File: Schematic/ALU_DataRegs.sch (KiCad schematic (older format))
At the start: 3 parts, among them IC4 74HCT574, IC5 74HCT574, IC6 M27C322-100F1

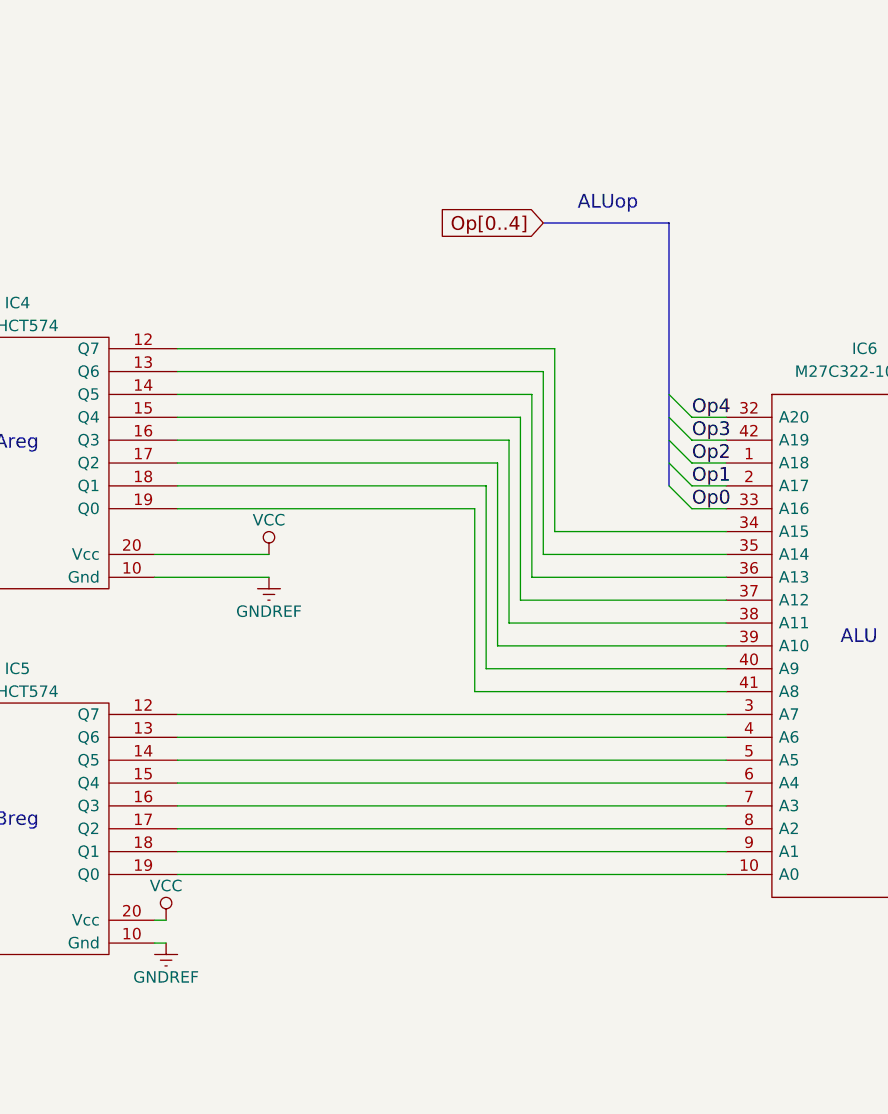
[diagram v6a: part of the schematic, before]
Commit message: Brought the PCB up to date with the new schematic, and tested the RAM with a test program.
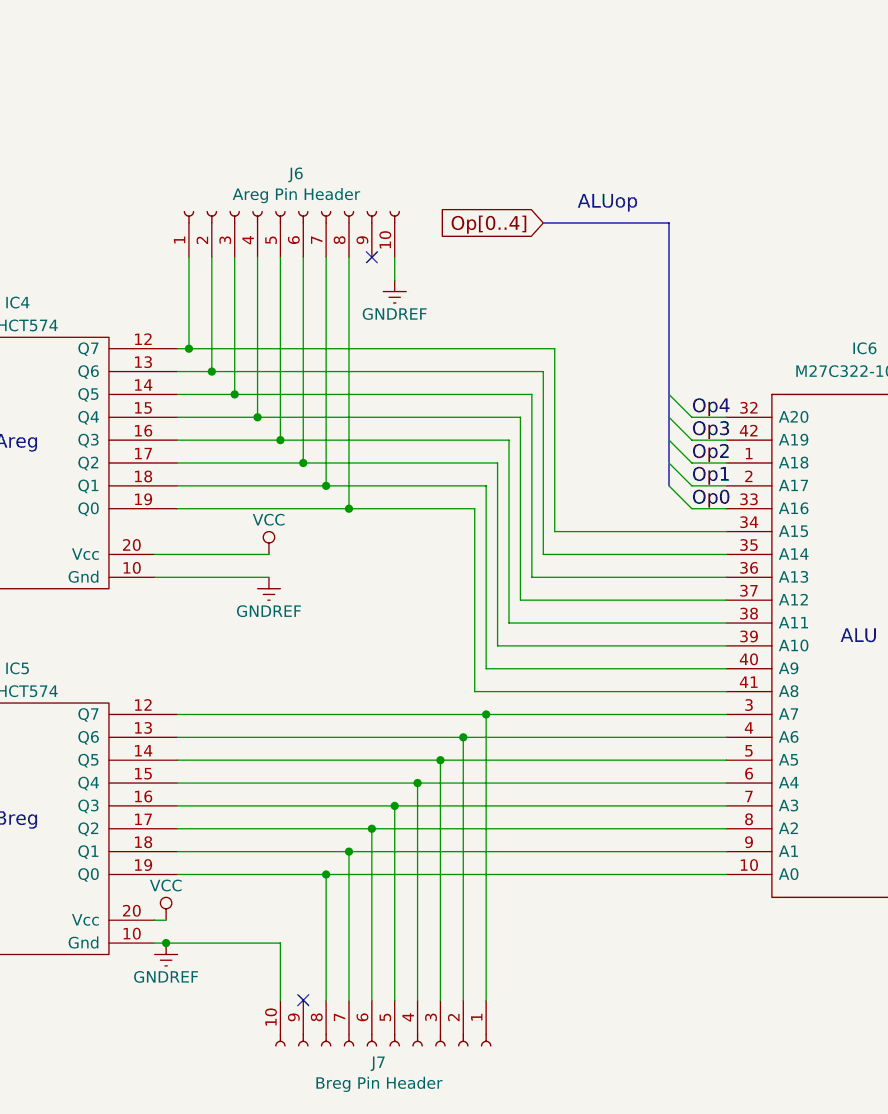
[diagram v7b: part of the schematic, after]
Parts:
- added J6: Areg Pin Header, Connector_PinSocket_2.54mm:PinSocket_1x10_P2.54mm_Vertical, symbol Connector:Conn_01x10_Female
- added J7: Breg Pin Header, Connector_PinSocket_2.54mm:PinSocket_1x10_P2.54mm_Vertical, symbol Connector:Conn_01x10_Female
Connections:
- net GNDREF: now also J6.10 (Pin_10), J7.10 (Pin_10)
- net at IC5.19 (Q0), IC6.10 (A0): now also J7.8 (Pin_8)
- net at IC5.12 (Q7), IC6.3 (A7): now also J7.1 (Pin_1)
- net at IC4.12 (Q7), IC6.34 (A15): now also J6.1 (Pin_1)
- net at IC4.13 (Q6), IC6.35 (A14): now also J6.2 (Pin_2)
- net at IC4.14 (Q5), IC6.36 (A13): now also J6.3 (Pin_3)
- net at IC4.15 (Q4), IC6.37 (A12): now also J6.4 (Pin_4)
- net at IC4.16 (Q3), IC6.38 (A11): now also J6.5 (Pin_5)
- net at IC4.17 (Q2), IC6.39 (A10): now also J6.6 (Pin_6)
- net at IC5.13 (Q6), IC6.4 (A6): now also J7.2 (Pin_2)
- net at IC4.18 (Q1), IC6.40 (A9): now also J6.7 (Pin_7)
- net at IC4.19 (Q0), IC6.41 (A8): now also J6.8 (Pin_8)
- net at IC5.14 (Q5), IC6.5 (A5): now also J7.3 (Pin_3)
- net at IC5.15 (Q4), IC6.6 (A4): now also J7.4 (Pin_4)
- net at IC5.16 (Q3), IC6.7 (A3): now also J7.5 (Pin_5)
- net at IC5.17 (Q2), IC6.8 (A2): now also J7.6 (Pin_6)
- net at IC5.18 (Q1), IC6.9 (A1): now also J7.7 (Pin_7)
- no-connect marks 3 -> 5
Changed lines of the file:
@@
 $EndComp
 Wire Wire Line
-	4500 4500 6900 4500
-Wire Wire Line
-	4500 4600 6900 4600
-Wire Wire Line
-	4500 4700 6900 4700
-Wire Wire Line
-	4500 4800 6900 4800
-Wire Wire Line
-	4500 4900 6900 4900
-Wire Wire Line
-	4500 5000 6900 5000
-Wire Wire Line
-	4500 5100 6900 5100
-Wire Wire Line
-	4500 5200 6900 5200
+	4500 4500 5850 4500
+Wire Wire Line
+	4500 4600 5750 4600
+Wire Wire Line
+	4500 4700 5650 4700
+Wire Wire Line
+	4500 4800 5550 4800
 Wire Wire Line
 	6150 3700 6900 3700
 Wire Wire Line
-	4500 2900 6150 2900
-Wire Wire Line
 	6100 3800 6900 3800
 Wire Wire Line
-	4500 3000 6100 3000
-Wire Wire Line
-	4500 3100 6050 3100
-Wire Wire Line
 	6050 3900 6900 3900
 Wire Wire Line
-	4500 3200 6000 3200
-Wire Wire Line
 	6000 4000 6900 4000
 Wire Wire Line
-	4500 3300 5950 3300
-Wire Wire Line
 	5950 4100 6900 4100
 Wire Wire Line
-	4500 3400 5900 3400
-Wire Wire Line
 	5900 4200 6900 4200
 Wire Wire Line
-	4500 3500 5850 3500
-Wire Wire Line
 	5850 4300 6900 4300
-Wire Wire Line
-	4500 3600 5800 3600
 Wire Wire Line
 	5800 4400 6900 4400
@@
 Wire Wire Line
 	8300 3300 8650 3300
+$Comp
+L Connector:Conn_01x10_Female J7
+U 1 1 5CD2E273
+P 5450 5950
+F 0 "J7" V 5523 5880 50  0000 C CNN
+F 1 "Breg Pin Header" V 5614 5880 50  0000 C CNN
+F 2 "Connector_PinSocket_2.54mm:PinSocket_1x10_P2.54mm_Vertical" H 5450 5950 50  0001 C CNN
+F 3 "~" H 5450 5950 50  0001 C CNN
+	1    5450 5950
+	0    1    1    0
+$EndComp
+Wire Wire Line
+	5850 5750 5850 4500
+Connection ~ 5850 4500
+Wire Wire Line
+	5850 4500 6900 4500
+Wire Wire Line
+	5750 5750 5750 4600
+Connection ~ 5750 4600
+Wire Wire Line
+	5750 4600 6900 4600
+Wire Wire Line
+	5650 5750 5650 4700
+Connection ~ 5650 4700
+Wire Wire Line
+	5650 4700 6900 4700
+Wire Wire Line
+	4500 5200 5150 5200
+Wire Wire Line
+	4500 5100 5250 5100
+Wire Wire Line
+	4500 5000 5350 5000
+Wire Wire Line
+	4500 4900 5450 4900
+Wire Wire Line
+	5550 5750 5550 4800
+Connection ~ 5550 4800
+Wire Wire Line
+	5550 4800 6900 4800
+Wire Wire Line
+	5450 5750 5450 4900
+Connection ~ 5450 4900
+Wire Wire Line
+	5450 4900 6900 4900
+Wire Wire Line
+	5350 5750 5350 5000
+Connection ~ 5350 5000
+Wire Wire Line
+	5350 5000 6900 5000
+Wire Wire Line
+	5250 5750 5250 5100
+Connection ~ 5250 5100
+Wire Wire Line
+	5250 5100 6900 5100
+Wire Wire Line
+	5150 5750 5150 5200
+Connection ~ 5150 5200
+Wire Wire Line
+	5150 5200 6900 5200
+NoConn ~ 5050 5750
+Wire Wire Line
+	4450 5500 4950 5500
+Wire Wire Line
+	4950 5500 4950 5750
+Connection ~ 4450 5500
+$Comp
+L Connector:Conn_01x10_Female J6
+U 1 1 5CD78577
+P 4950 2300
+F 0 "J6" V 5115 2230 50  0000 C CNN
+F 1 "Areg Pin Header" V 5024 2230 50  0000 C CNN
+F 2 "Connector_PinSocket_2.54mm:PinSocket_1x10_P2.54mm_Vertical" H 4950 2300 50  0001 C CNN
+F 3 "~" H 4950 2300 50  0001 C CNN
+	1    4950 2300
+	0    -1   -1   0
+$EndComp
+NoConn ~ 5350 2500
+$Comp
+L power:GNDREF #PWR0103
+U 1 1 5CDA8761
+P 5450 2600
+F 0 "#PWR0103" H 5450 2350 50  0001 C CNN
+F 1 "GNDREF" H 5450 2450 50  0000 C CNN
+F 2 "" H 5450 2600 50  0001 C CNN
+F 3 "" H 5450 2600 50  0001 C CNN
+	1    5450 2600
+	1    0    0    -1
+$EndComp
+Wire Wire Line
+	5450 2500 5450 2600
+Wire Wire Line
+	4500 3600 5250 3600
+Wire Wire Line
+	4500 3500 5150 3500
+Wire Wire Line
+	4500 3400 5050 3400
+Wire Wire Line
+	4500 3300 4950 3300
+Wire Wire Line
+	4500 3200 4850 3200
+Wire Wire Line
+	4500 3100 4750 3100
+Wire Wire Line
+	4500 3000 4650 3000
+Wire Wire Line
+	4500 2900 4550 2900
+Wire Wire Line
+	4550 2500 4550 2900
+Connection ~ 4550 2900
+Wire Wire Line
+	4550 2900 6150 2900
+Wire Wire Line
+	4650 2500 4650 3000
+Connection ~ 4650 3000
+Wire Wire Line
+	4650 3000 6100 3000
+Wire Wire Line
+	4750 2500 4750 3100
+Connection ~ 4750 3100
+Wire Wire Line
+	4750 3100 6050 3100
+Wire Wire Line
+	4850 2500 4850 3200
+Connection ~ 4850 3200
+Wire Wire Line
+	4850 3200 6000 3200
+Wire Wire Line
+	4950 2500 4950 3300
+Connection ~ 4950 3300
+Wire Wire Line
+	4950 3300 5950 3300
+Wire Wire Line
+	5050 2500 5050 3400
+Connection ~ 5050 3400
+Wire Wire Line
+	5050 3400 5900 3400
+Wire Wire Line
+	5150 2500 5150 3500
+Connection ~ 5150 3500
+Wire Wire Line
+	5150 3500 5850 3500
+Wire Wire Line
+	5250 2500 5250 3600
 Wire Bus Line
 	6650 2350 6650 3500
@@
 Wire Bus Line
 	2750 3000 2750 5300
+Connection ~ 5250 3600
+Wire Wire Line
+	5250 3600 5800 3600
 $EndSCHEMATC
